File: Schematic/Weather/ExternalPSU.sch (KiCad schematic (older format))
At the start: 3 parts, among them J7 3_Way_Wire

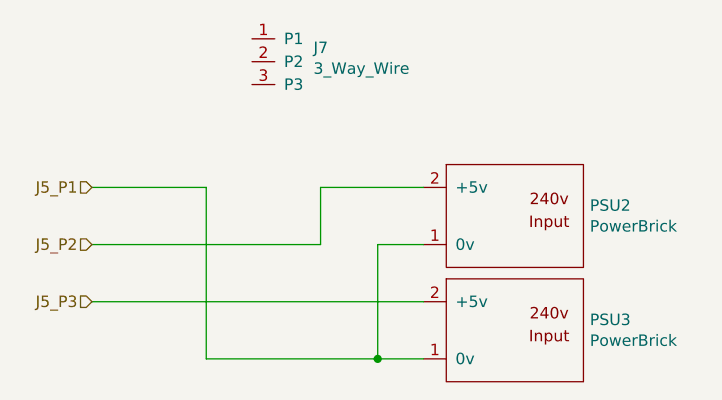
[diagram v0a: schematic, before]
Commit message: Connector changes
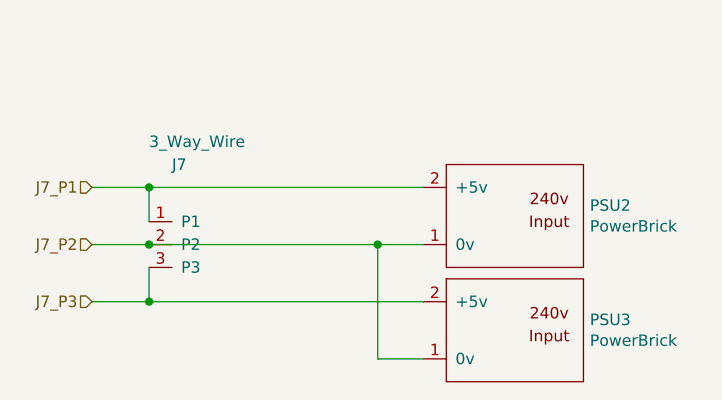
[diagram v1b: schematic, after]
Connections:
- net J5_P1 is gone; now on net J7_P2: PSU2.1 (0v), PSU3.1 (0v)
- net J5_P2 is gone; now on net J7_P1: PSU2.2 (+5v)
- net J5_P3 is gone; now on net J7_P3: PSU3.2 (+5v)
- net J7_P1: now reaches J7.1 (P1)
- net J7_P2: now reaches J7.2 (P2)
- net J7_P3: now reaches J7.3 (P3)
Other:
- moved on the sheet: J7
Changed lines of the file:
@@
 $EndDescr
 Text HLabel 2500 2000 0    50   Input ~ 0
-J5_P1
+J7_P1
 Text HLabel 2500 2250 0    50   Input ~ 0
-J5_P2
+J7_P2
 Text HLabel 2500 2500 0    50   Input ~ 0
-J5_P3
+J7_P3
 $Comp
 L MyComponents:PowerBrick PSU2
@@
 $EndComp
 Wire Wire Line
-	2500 2250 3500 2250
-Wire Wire Line
-	3500 2250 3500 2000
-Wire Wire Line
-	3500 2000 3950 2000
-Wire Wire Line
-	2500 2000 3000 2000
-Wire Wire Line
-	3000 2000 3000 2750
-Wire Wire Line
-	3000 2750 3750 2750
+	2500 2250 2750 2250
 Wire Wire Line
 	3950 2250 3750 2250
 Wire Wire Line
 	3750 2250 3750 2750
-Connection ~ 3750 2750
 Wire Wire Line
 	3750 2750 3950 2750
 Wire Wire Line
-	3950 2500 2500 2500
+	3950 2500 2750 2500
 $Comp
 L MyComponents:3_Way_Wire J7
 U 1 1 5CB57954
-P 3300 1350
-F 0 "J7" H 3469 1311 50  0000 L CNN
-F 1 "3_Way_Wire" H 3469 1220 50  0000 L CNN
-F 2 "Connector_PinHeader_2.54mm:PinHeader_1x03_P2.54mm_Vertical" H 3300 1350 50  0001 C CNN
-F 3 "" H 3300 1350 50  0001 C CNN
-	1    3300 1350
+P 2850 2150
+F 0 "J7" H 2850 2400 50  0000 L CNN
+F 1 "3_Way_Wire" H 2750 2500 50  0000 L CNN
+F 2 "Connector_PinHeader_2.54mm:PinHeader_1x03_P2.54mm_Vertical" H 2850 2150 50  0001 C CNN
+F 3 "" H 2850 2150 50  0001 C CNN
+	1    2850 2150
 	1    0    0    -1
 $EndComp
+Wire Wire Line
+	2750 2250 3750 2250
+Connection ~ 2750 2250
+Connection ~ 3750 2250
+Wire Wire Line
+	2500 2000 2750 2000
+Wire Wire Line
+	2750 2000 2750 2150
+Wire Wire Line
+	3950 2000 2750 2000
+Connection ~ 2750 2000
+Wire Wire Line
+	2750 2350 2750 2500
+Connection ~ 2750 2500
+Wire Wire Line
+	2750 2500 2500 2500
 $EndSCHEMATC
